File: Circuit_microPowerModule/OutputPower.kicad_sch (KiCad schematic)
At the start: 36 parts, among them J101 Screw_Terminal_01x02, Q401 RU1C002ZP, Q402 RK7002BM, U404 MP2315S, U405 LM358

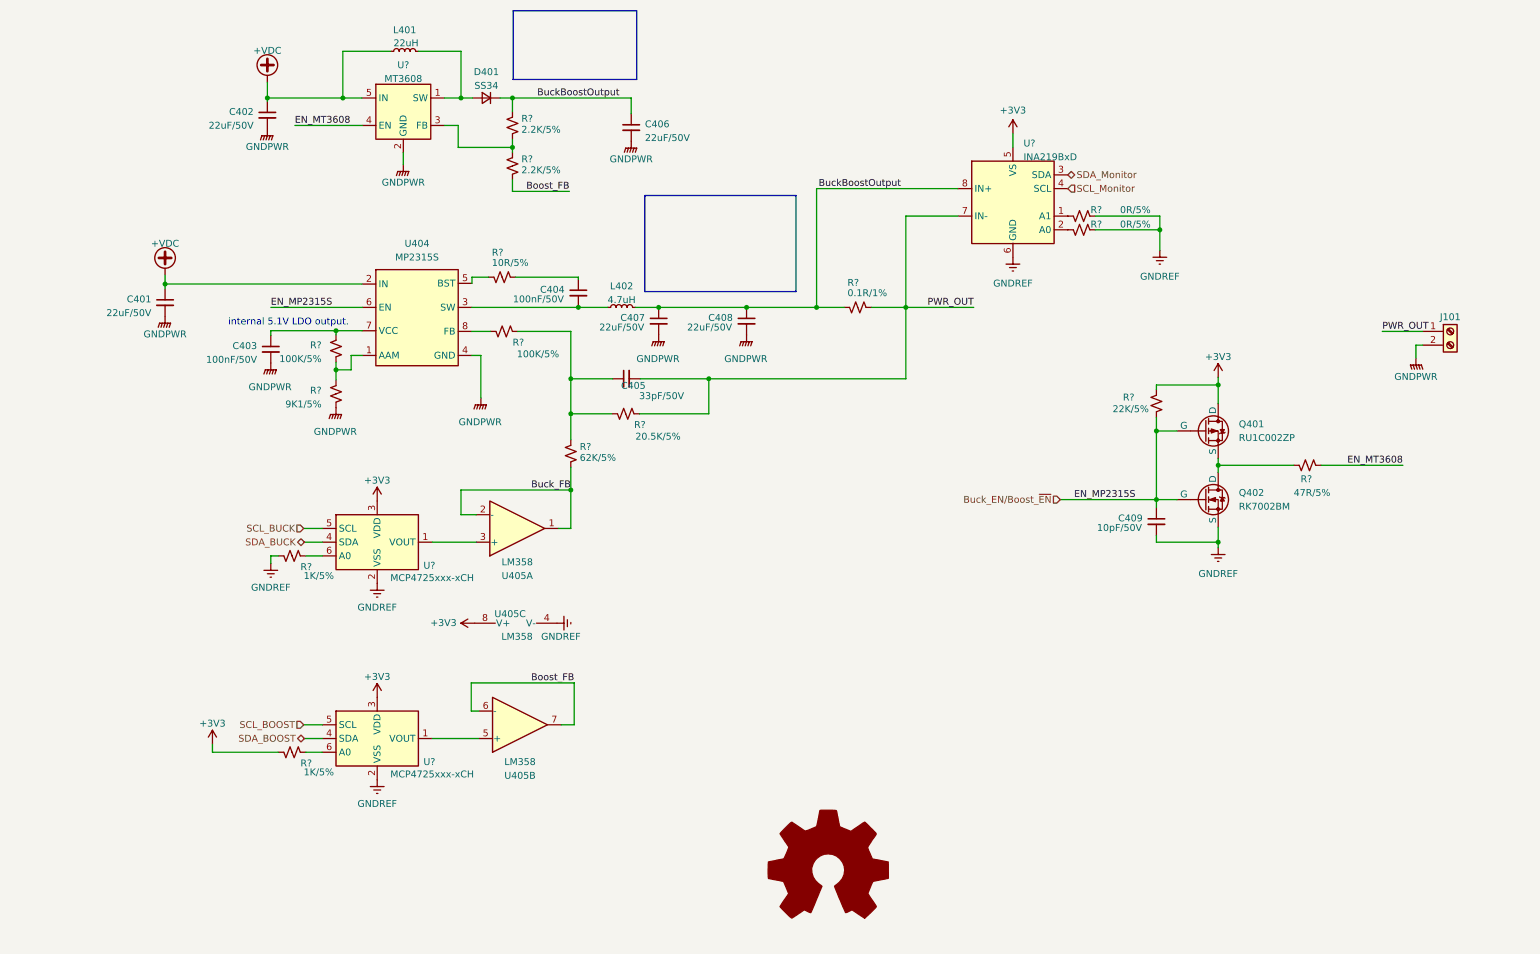
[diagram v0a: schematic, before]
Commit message: added H-Bridge
Control load forward or reverse (current direction)
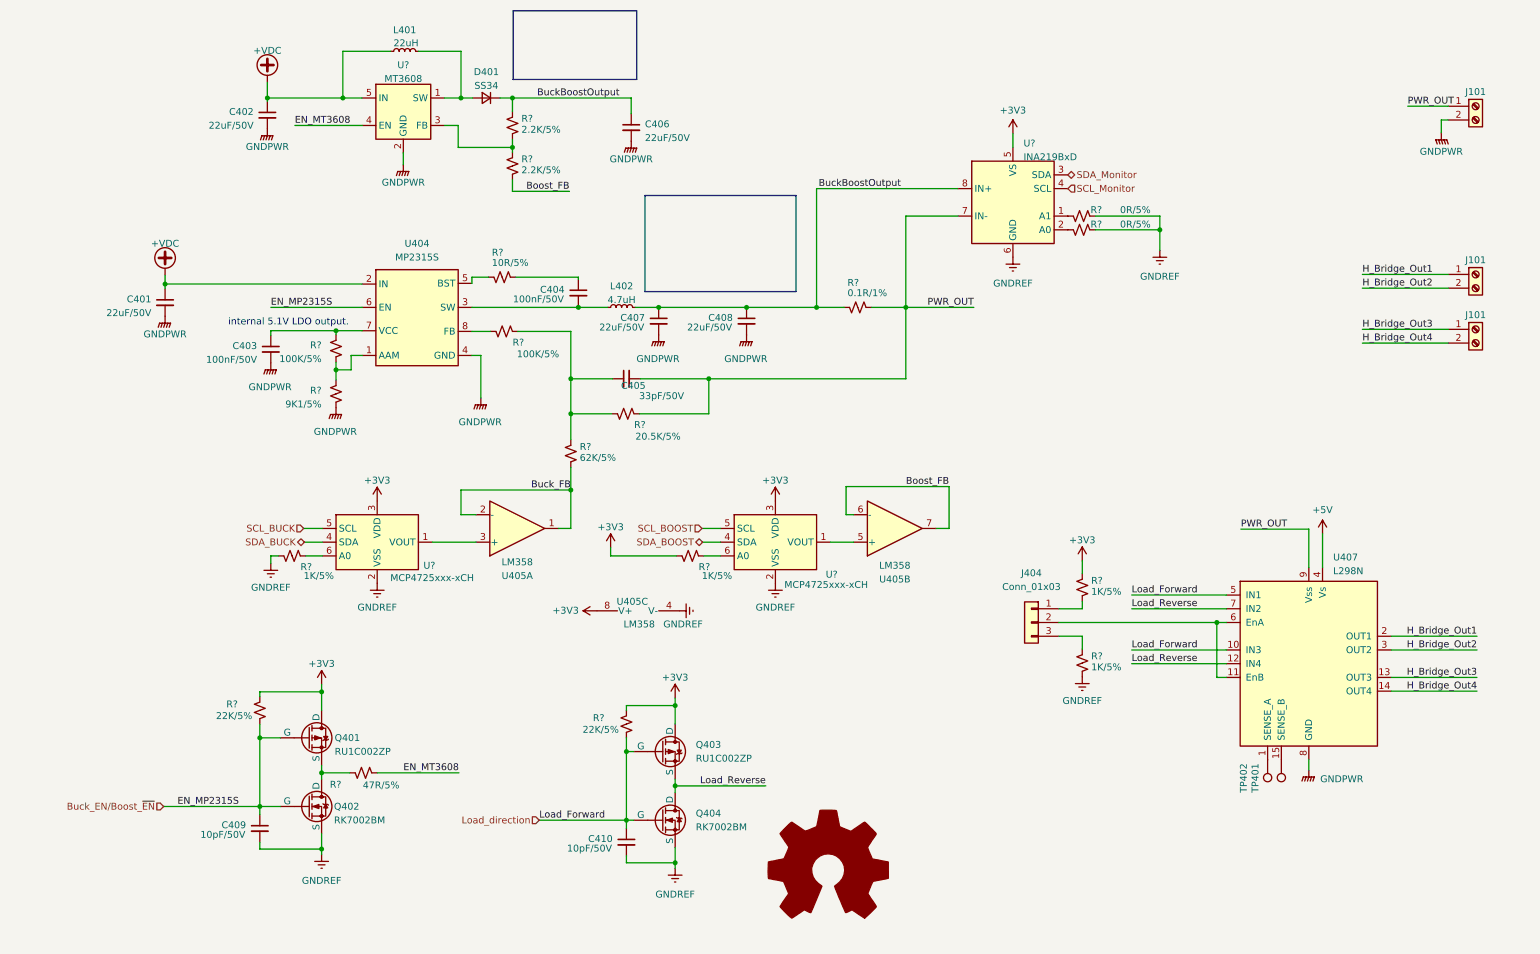
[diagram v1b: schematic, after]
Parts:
- added C410: 10pF/50V, symbol Device:C_Small
- added J101 (x2): Screw_Terminal_01x02, Connector_Phoenix_MC:PhoenixContact_MC_1,5_2-G-3.81_1x02_P3.81mm_Horizontal, symbol Connector:Screw_Terminal_01x02
- added J404: Conn_01x03, Connector_PinHeader_2.54mm:PinHeader_1x03_P2.54mm_Vertical, symbol Connector_Generic:Conn_01x03
- added Q403: RU1C002ZP, symbol Simulation_SPICE:PMOS
- added Q404: RK7002BM, symbol Simulation_SPICE:NMOS
- added R? (x2): 1K/5%, Resistor_SMD:R_0603_1608Metric, symbol Device:R_Small_US
- added R?: 22K/5%, Resistor_SMD:R_0603_1608Metric, symbol Device:R_Small_US
- added TP401, TP402: TestPoint, symbol Connector:TestPoint
- added U407: L298N, Package_TO_SOT_THT:TO-220-15_P2.54x2.54mm_StaggerOdd_Lead4.58mm_Vertical, symbol Driver_Motor:L298N
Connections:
- net +3V3: now also Q403.1 (D), R?.1, R?.2
- net GNDPWR: now also U407.8 (GND)
- net GNDREF: now also C410.2, Q404.3 (S), R?.2
- net PWR_OUT: now also U407.9 (Vss)
- new net: J404.1 (Pin_1), R?.2
- new net: J404.2 (Pin_2), U407.11 (EnB), U407.6 (EnA)
- new net: J404.3 (Pin_3), R?.1
- new net: TP401.1, U407.15 (SENSE_B)
- new net: TP402.1, U407.1 (SENSE_A)
- new net +5V: U407.4 (Vs)
- new net H_Bridge_Out1: J101.1 (Pin_1), U407.2 (OUT1)
- new net H_Bridge_Out2: J101.2 (Pin_2), U407.3 (OUT2)
- new net H_Bridge_Out3: J101.1 (Pin_1), U407.13 (OUT3)
- new net H_Bridge_Out4: J101.2 (Pin_2), U407.14 (OUT4)
- new net Load_Reverse: Q403.3 (S), Q404.1 (D), U407.12 (IN4), U407.7 (IN2)
- new net Load_direction: C410.1, Q403.2 (G), Q404.2 (G), R?.1, U407.10 (IN3), U407.5 (IN1)
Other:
- moved on the sheet: C409, J101, Q401, Q402, R?, U405B, U405C, U?

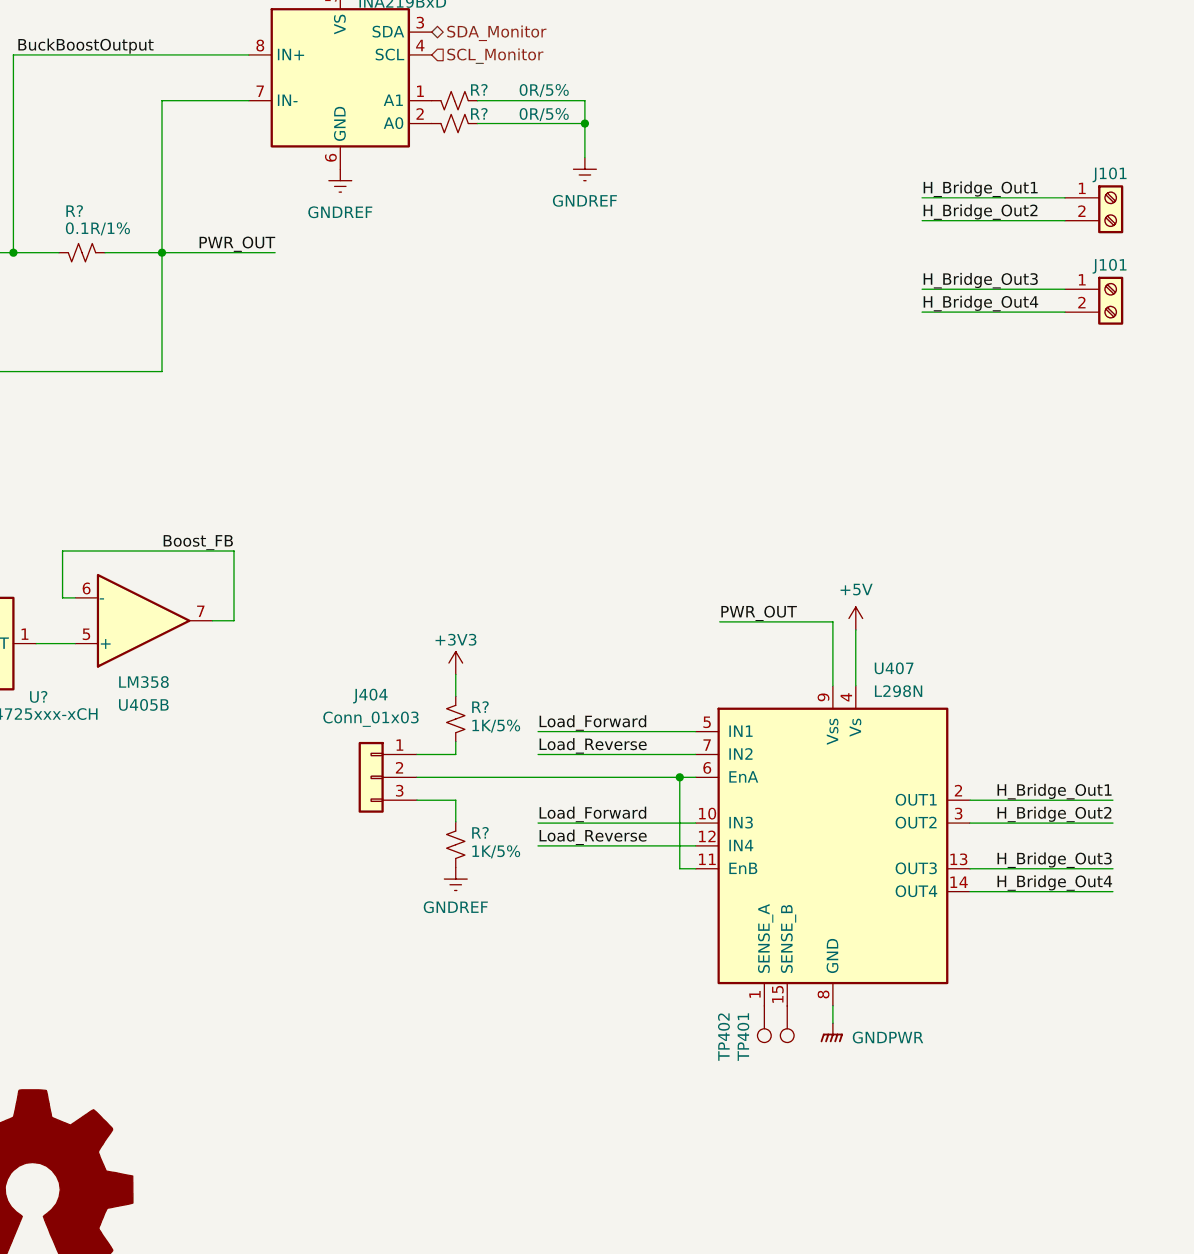
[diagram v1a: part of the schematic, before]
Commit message: modify ERC error, protect components
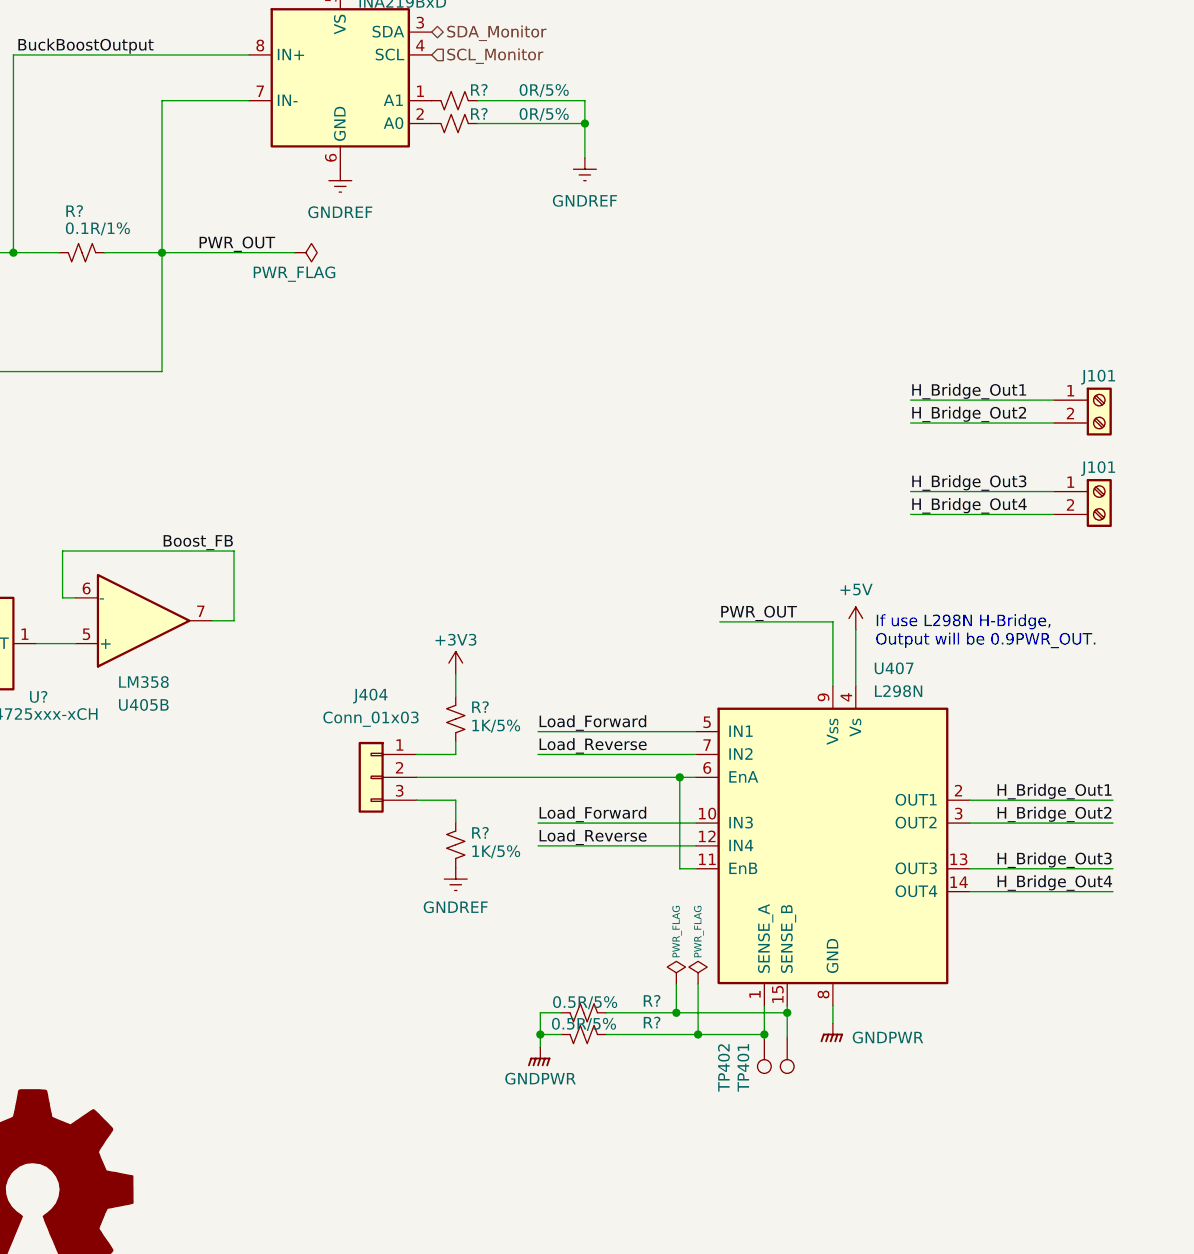
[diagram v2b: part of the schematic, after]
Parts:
- added R? (x2): 0.5R/5%, Resistor_SMD:R_2512_6332Metric, symbol Device:R_Small_US
- Q401, Q402, Q403, Q404: footprint (none) -> Package_TO_SOT_SMD:SOT-23-3
- TP401, TP402: footprint (none) -> TestPoint:TestPoint_Pad_D2.5mm
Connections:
- net GNDPWR: now also R?.2, R?.2
- net at TP401.1, U407.15 (SENSE_B): now also R?.1
- net at TP402.1, U407.1 (SENSE_A): now also R?.1
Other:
- note added: "If use L298N H-Bridge, Output will be 0.9PWR_OUT."
- title: (none) -> µPower Module
- moved on the sheet: J101, TP401, TP402

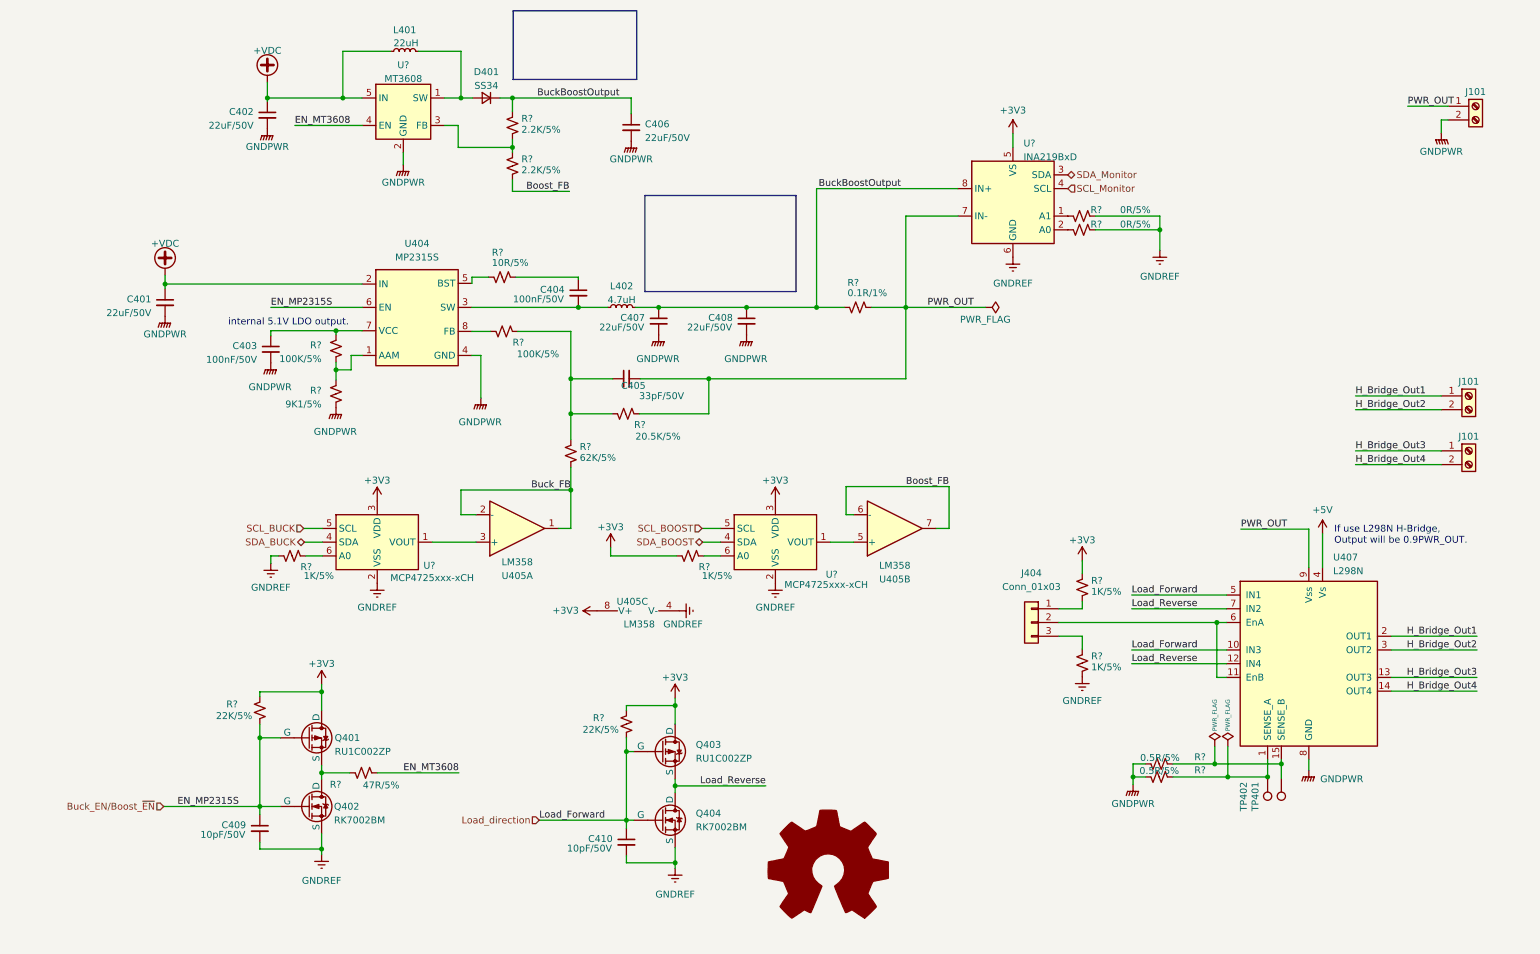
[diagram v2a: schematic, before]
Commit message: modify ERC warning
modify OPA, TVS-Diode, Cap
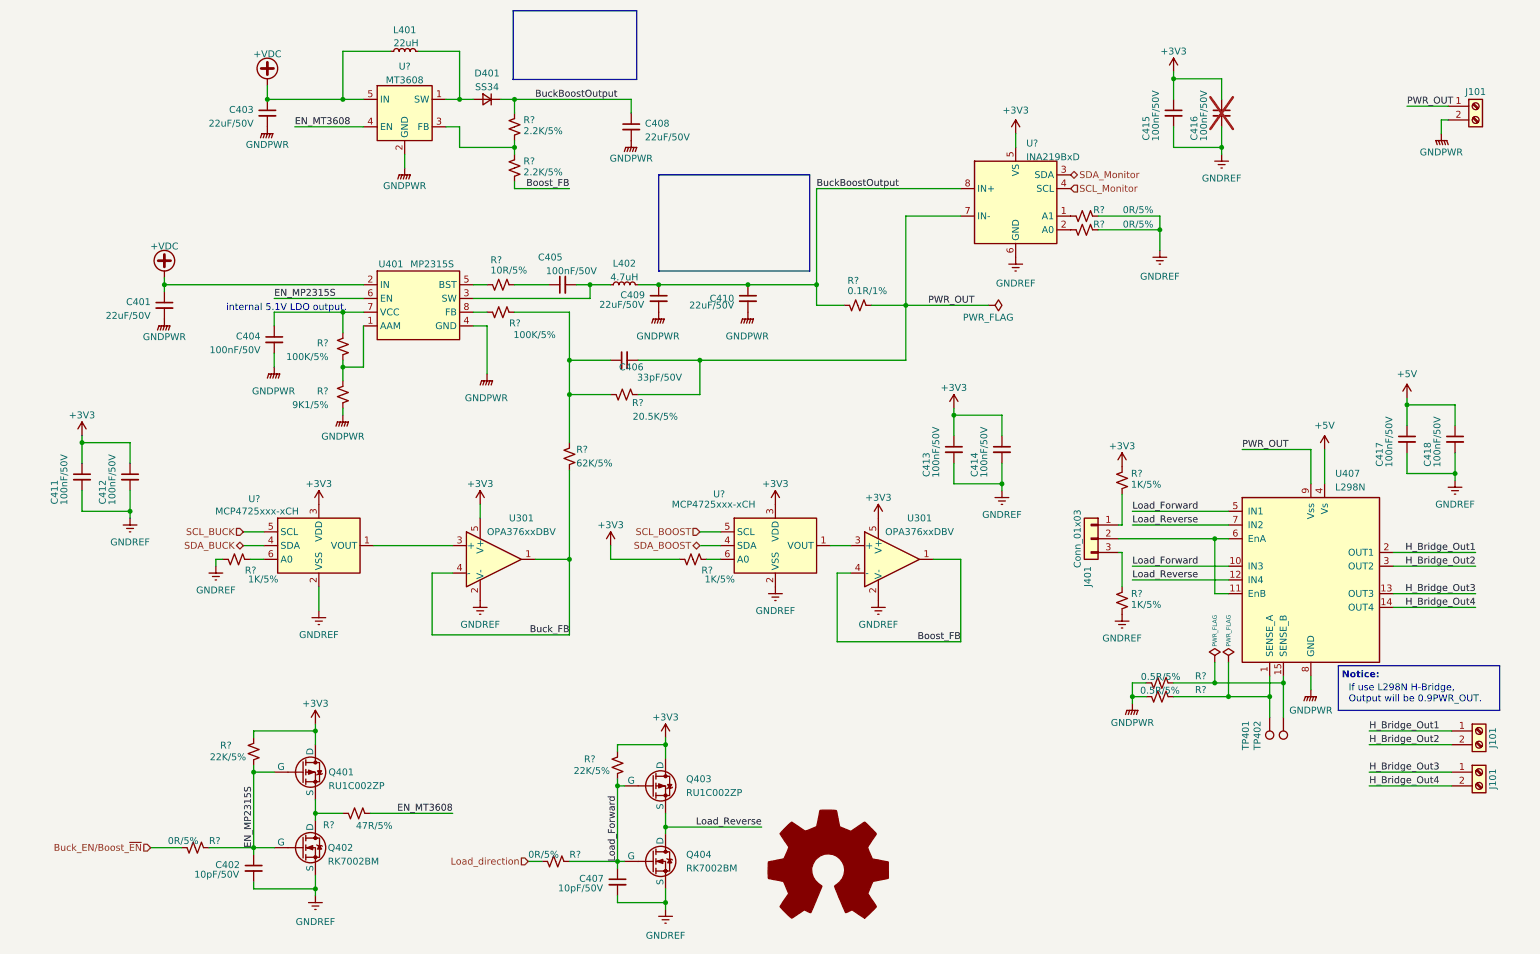
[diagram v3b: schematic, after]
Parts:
- removed U405: LM358, Package_TO_SOT_SMD:TSOT-23-8, symbol Amplifier_Operational:LM358
- added C411, C412, C413, C414, C415, C416, C417, C418: 100nF/50V, Capacitor_SMD:C_0603_1608Metric, symbol Device:C_Small
- added R? (x2): 0R/5%, Resistor_SMD:R_0603_1608Metric, symbol Device:R_Small_US
- added U301 (x2): OPA376xxDBV, Package_TO_SOT_SMD:SOT-23-5, symbol Amplifier_Operational:OPA376xxDBV
- C401: footprint (none) -> Capacitor_SMD:C_1206_3216Metric
- C402: renamed from C409; footprint (none) -> Capacitor_SMD:C_0603_1608Metric
- C403: renamed from C402; footprint (none) -> Capacitor_SMD:C_1206_3216Metric
- C407: renamed from C410; footprint (none) -> Capacitor_SMD:C_0603_1608Metric
- C408: renamed from C406; footprint (none) -> Capacitor_SMD:C_1206_3216Metric
- C409: renamed from C407; footprint (none) -> Capacitor_SMD:C_1206_3216Metric
- C410: renamed from C408; footprint (none) -> Capacitor_SMD:C_1206_3216Metric
- renumbered C403 to C404, C404 to C405, C405 to C406, J404 to J401, TP402 to TP401, TP401 to TP402, U404 to U401
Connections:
- net +3V3: now also C411.1, C412.1, C413.1, C414.1, C415.1, C416.1, U301.5 (V+), U301.5 (V+)
- net +5V: now also C417.1, C418.1
- net Boost_FB: now also U301.1, U301.4 (-)
- net Buck_EN/Boost_~{EN}: now also R?.1; no longer C402.1, Q401.2 (G), Q402.2 (G), R?.1, U401.6 (EN)
- net Buck_FB: now also U301.1, U301.4 (-)
- net GNDREF: now also C411.2, C412.2, C413.2, C414.2, C415.2, C416.2, C417.2, C418.2, U301.2 (V-), U301.2 (V-)
- net Load_direction: now also R?.1; no longer C407.1, Q403.2 (G), Q404.2 (G), R?.1, U407.10 (IN3), U407.5 (IN1)
- net at U?.1 (VOUT): now also U301.3 (+) (x2)
- new net EN_MP2315S: C402.1, Q401.2 (G), Q402.2 (G), R?.1, R?.2, U401.6 (EN)
- new net Load_Forward: C407.1, Q403.2 (G), Q404.2 (G), R?.1, R?.2, U407.10 (IN3), U407.5 (IN1)
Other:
- note added: "Notice:"
- moved on the sheet: C401, C402, C404, C405, C406, C407, C409, C410, J101, J401, L402, Q401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
